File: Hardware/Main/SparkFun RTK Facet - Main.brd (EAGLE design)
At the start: 60 x 43 mm, 126 parts, among them J1 QWIIC_RIGHT_ANGLE, J2 U.FL, J9 CORTEX_JTAG_DEBUG_PTH, Q2 MBT3904DW1T1, Q3 SIL2308, U1 74HC4052D, U10 MCP73833, U12 AP2112K-3.3, U2 3.3V, U3 U-BLOX_ZED-F9P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

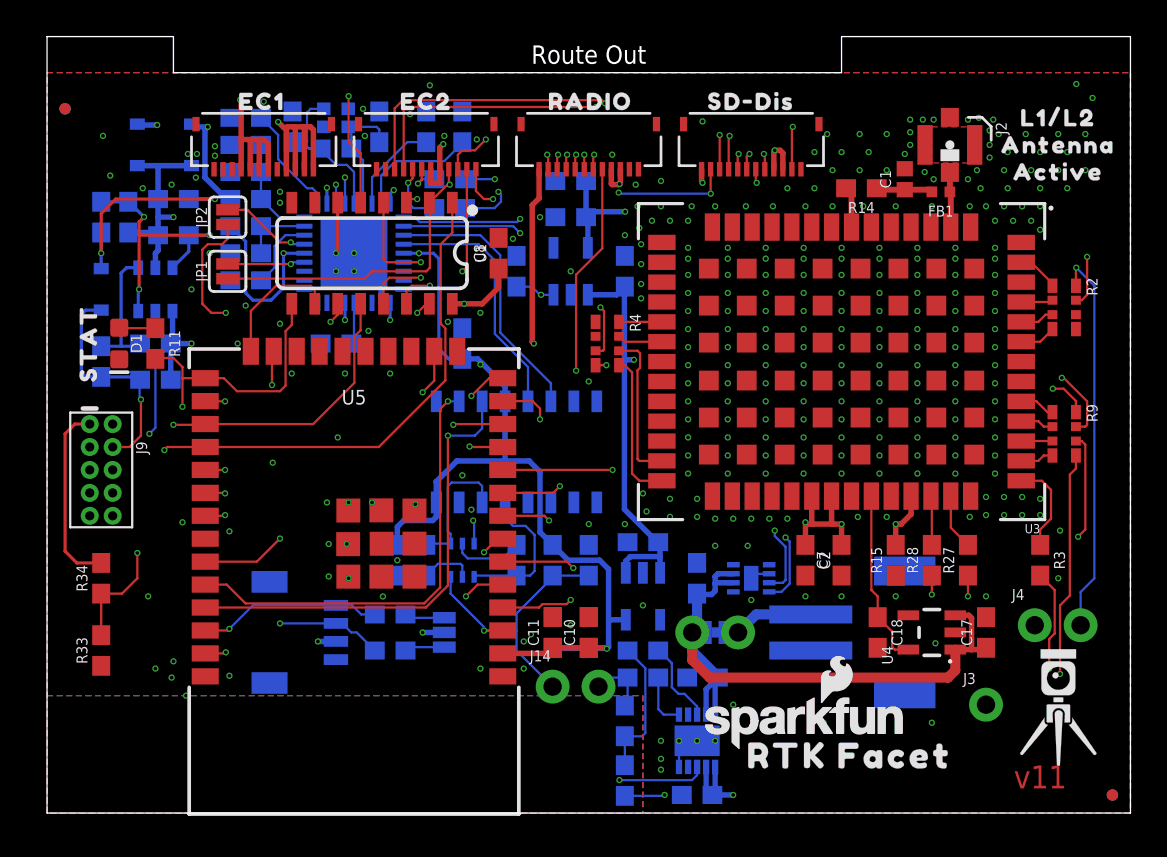
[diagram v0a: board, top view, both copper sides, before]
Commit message: Reduce Main, Connector, Display, and Cell board widths by 1mm to allow for v-score protrusion.
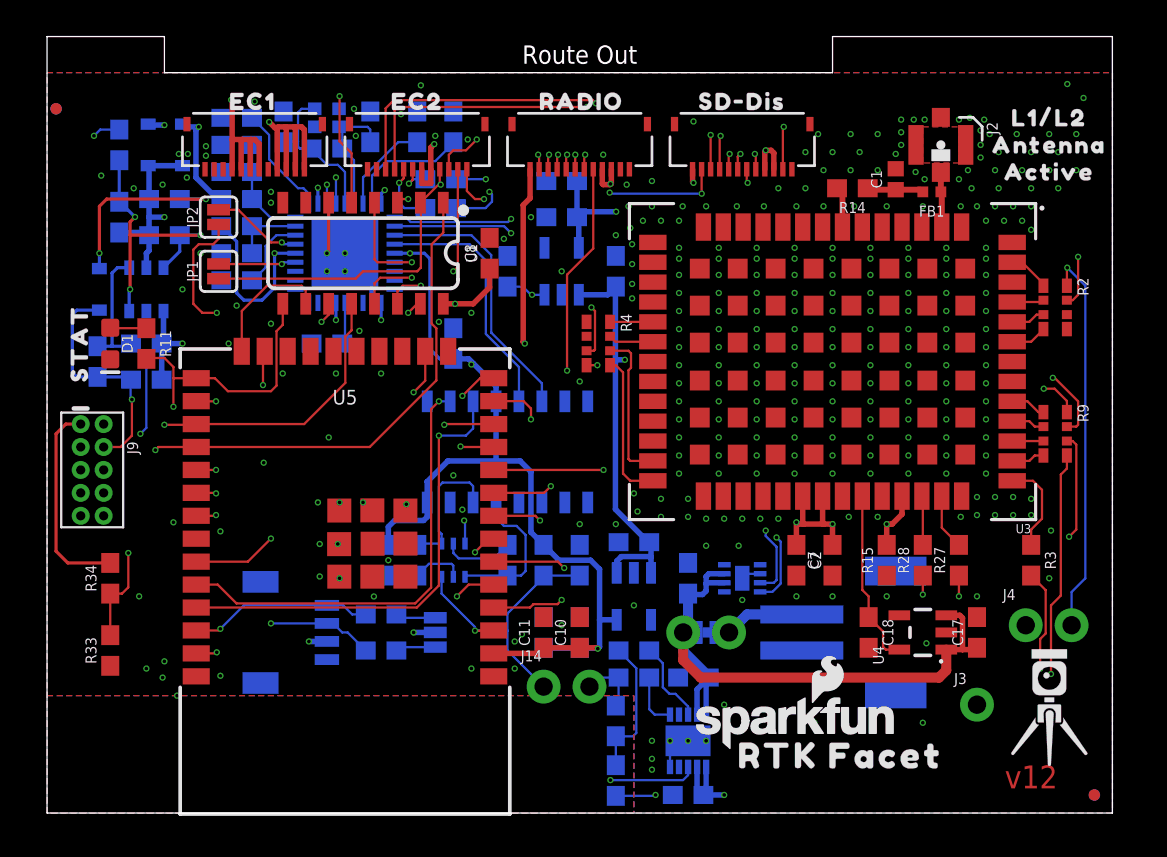
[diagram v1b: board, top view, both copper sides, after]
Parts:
- moved C23 4.12 mm to (4.00, 37.0), turned to 270 degrees
- moved JP21 1.00 mm to (58.0, 1.00)
- moved JP71 1.00 mm to (58.0, 1.00)
- moved D7 0.60 mm to (5.60, 37.0)
- moved C1 0.50 mm to (47.0, 35.1)
- moved C10 0.50 mm to (29.5, 10.0)
- moved C11 0.50 mm to (27.5, 10.0)
- moved C12 0.50 mm to (29.5, 14.0)
- moved C13 0.50 mm to (18.9, 14.0)
- moved C14 0.50 mm to (22.5, 26.0)
- moved C15 0.50 mm to (35.5, 13.0)
- moved C16 0.50 mm to (35.5, 1.00)
- moved C17 0.50 mm to (51.5, 10.0)
- moved C18 0.50 mm to (45.5, 10.0)
- moved C19 0.50 mm to (13.1, 38.0)
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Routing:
- net V_RAW: track 78.3 -> 77.2 mm
- net ESP_3V3: track 118.6 -> 119.6 mm
- net N$6: track 15.3 -> 16.1 mm
- net ESP_I35/DEVICE_SENSE: track 27.4 -> 26.7 mm
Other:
- board size 60 x 43 mm -> 59 x 43 mm
- board text added: "v12"
- board text removed: "v11"

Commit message: Add revisions to schematics. Add PDFs of schematics.
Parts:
- moved FRAME1 0.62 mm to (82.5, 6.35)
- moved FRAME2 0.62 mm to (82.5, 6.35)
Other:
- board text added: "N. Seidle"
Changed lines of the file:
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@@
 <layers>
 <layer number="1" name="Top/Horz" color="4" fill="1" visible="yes" active="yes"/>
-<layer number="2" name="GND/Horz" color="1" fill="3" visible="yes" active="yes"/>
-<layer number="15" name="3.3V/Vert" color="4" fill="6" visible="yes" active="yes"/>
+<layer number="2" name="GND/Horz" color="1" fill="3" visible="no" active="yes"/>
+<layer number="15" name="3.3V/Vert" color="4" fill="6" visible="no" active="yes"/>
 <layer number="16" name="Bottom/Vert" color="1" fill="1" visible="yes" active="yes"/>
 <layer number="17" name="Pads" color="2" fill="1" visible="yes" active="yes"/>
@@
 <layer number="23" name="tOrigins" color="15" fill="1" visible="yes" active="yes"/>
 <layer number="24" name="bOrigins" color="15" fill="1" visible="yes" active="yes"/>
-<layer number="25" name="tNames" color="7" fill="1" visible="yes" active="yes"/>
-<layer number="26" name="bNames" color="7" fill="1" visible="yes" active="yes"/>
-<layer number="27" name="tValues" color="7" fill="1" visible="yes" active="yes"/>
-<layer number="28" name="bValues" color="7" fill="1" visible="yes" active="yes"/>
-<layer number="29" name="tStop" color="7" fill="3" visible="yes" active="yes"/>
-<layer number="30" name="bStop" color="7" fill="6" visible="yes" active="yes"/>
-<layer number="31" name="tCream" color="7" fill="4" visible="yes" active="yes"/>
-<layer number="32" name="bCream" color="7" fill="5" visible="yes" active="yes"/>
-<layer number="33" name="tFinish" color="6" fill="3" visible="yes" active="yes"/>
-<layer number="34" name="bFinish" color="6" fill="6" visible="yes" active="yes"/>
-<layer number="35" name="tGlue" color="7" fill="4" visible="yes" active="yes"/>
-<layer number="36" name="bGlue" color="7" fill="5" visible="yes" active="yes"/>
-<layer number="37" name="tTest" color="7" fill="1" visible="yes" active="yes"/>
-<layer number="38" name="bTest" color="7" fill="1" visible="yes" active="yes"/>
-<layer number="39" name="tKeepout" color="4" fill="11" visible="yes" active="yes"/>
-<layer number="40" name="bKeepout" color="1" fill="11" visible="yes" active="yes"/>
-<layer number="41" name="tRestrict" color="4" fill="10" visible="yes" active="yes"/>
-<layer number="42" name="bRestrict" color="1" fill="10" visible="yes" active="yes"/>
-<layer number="43" name="vRestrict" color="2" fill="10" visible="yes" active="yes"/>
-<layer number="44" name="Drills" color="7" fill="1" visible="yes" active="yes"/>
+<layer number="25" name="tNames" color="7" fill="1" visible="no" active="yes"/>
+<layer number="26" name="bNames" color="7" fill="1" visible="no" active="yes"/>
+<layer number="27" name="tValues" color="7" fill="1" visible="no" active="yes"/>
+<layer number="28" name="bValues" color="7" fill="1" visible="no" active="yes"/>
+<layer number="29" name="tStop" color="7" fill="3" visible="no" active="yes"/>
+<layer number="30" name="bStop" color="7" fill="6" visible="no" active="yes"/>
+<layer number="31" name="tCream" color="7" fill="4" visible="no" active="yes"/>
+<layer number="32" name="bCream" color="7" fill="5" visible="no" active="yes"/>
+<layer number="33" name="tFinish" color="6" fill="3" visible="no" active="yes"/>
+<layer number="34" name="bFinish" color="6" fill="6" visible="no" active="yes"/>
+<layer number="35" name="tGlue" color="7" fill="4" visible="no" active="yes"/>
+<layer number="36" name="bGlue" color="7" fill="5" visible="no" active="yes"/>
+<layer number="37" name="tTest" color="7" fill="1" visible="no" active="yes"/>
+<layer number="38" name="bTest" color="7" fill="1" visible="no" active="yes"/>
+<layer number="39" name="tKeepout" color="4" fill="11" visible="no" active="yes"/>
+<layer number="40" name="bKeepout" color="1" fill="11" visible="no" active="yes"/>
+<layer number="41" name="tRestrict" color="4" fill="10" visible="no" active="yes"/>
+<layer number="42" name="bRestrict" color="1" fill="10" visible="no" active="yes"/>
+<layer number="43" name="vRestrict" color="2" fill="10" visible="no" active="yes"/>
+<layer number="44" name="Drills" color="7" fill="1" visible="no" active="yes"/>
 <layer number="45" name="Holes" color="7" fill="1" visible="yes" active="yes"/>
-<layer number="46" name="Milling" color="3" fill="1" visible="yes" active="yes"/>
-<layer number="47" name="Measures" color="7" fill="1" visible="yes" active="yes"/>
-<layer number="48" name="Document" color="7" fill="1" visible="yes" active="yes"/>
-<layer number="49" name="Reference" color="7" fill="1" visible="yes" active="yes"/>
-<layer number="50" name="dxf" color="7" fill="1" visible="yes" active="yes"/>
+<layer number="46" name="Milling" color="3" fill="1" visible="no" active="yes"/>
+<layer number="47" name="Measures" color="7" fill="1" visible="no" active="yes"/>
+<layer number="48" name="Document" color="7" fill="1" visible="no" active="yes"/>
+<layer number="49" name="Reference" color="7" fill="1" visible="no" active="yes"/>
+<layer number="50" name="dxf" color="7" fill="1" visible="no" active="yes"/>
 <layer number="51" name="tDocu" color="6" fill="1" visible="yes" active="yes"/>
-<layer number="52" name="bDocu" color="7" fill="1" visible="yes" active="yes"/>
+<layer number="52" name="bDocu" color="7" fill="1" visible="no" active="yes"/>
 <layer number="91" name="Nets" color="2" fill="1" visible="no" active="no"/>
 <layer number="92" name="Busses" color="1" fill="1" visible="no" active="no"/>
@@
 <text x="29.5" y="42" size="1.016" layer="20" font="vector" ratio="15" align="center">Route Out</text>
 <text x="63.81" y="60.96" size="1.778" layer="51" font="vector" ratio="15">Impedance controlled: JLC7628</text>
+<text x="113.03" y="6.35" size="1.778" layer="51" font="vector" ratio="15">N. Seidle</text>
 </plain>
 <attributes>
@@
 </element>
 <element name="U$30" library="SparkFun-Aesthetics" package="QWIIC_4MM" value="" x="13" y="14.6" smashed="yes" rot="MR0"/>
-<element name="FRAME2" library="SparkFun-Aesthetics" package="CREATIVE_COMMONS" value="FRAME-LEDGER" x="82.04" y="6" smashed="yes">
-<attribute name="DESIGNER" value="" x="82.04" y="6" size="1.778" layer="27" font="vector" ratio="15" display="off"/>
-<attribute name="REV" value="" x="82.04" y="6" size="1.778" layer="27" font="vector" ratio="15" display="off"/>
+<element name="FRAME2" library="SparkFun-Aesthetics" package="CREATIVE_COMMONS" value="FRAME-LEDGER" x="82.55" y="6.35" smashed="yes">
+<attribute name="DESIGNER" value="" x="82.55" y="6.35" size="1.778" layer="27" font="vector" ratio="15" display="off"/>
+<attribute name="REV" value="" x="82.55" y="6.35" size="1.778" layer="27" font="vector" ratio="15" display="off"/>
 </element>
 <element name="R9" library="SparkFun-Resistors" package="1206_RA" value="33" x="55.8" y="21" smashed="yes" rot="R270">
@@
 <attribute name="VALUE" x="6.5" y="33.238" size="0.6096" layer="28" font="vector" ratio="20" rot="MR0" align="top-center"/>
 </element>
-<element name="FRAME1" library="SparkFun-Aesthetics" package="CREATIVE_COMMONS" value="FRAME-LEDGER" x="82.04" y="6" smashed="yes">
-<attribute name="DESIGNER" value="" x="82.04" y="6" size="1.778" layer="27" font="vector" ratio="15" display="off"/>
-<attribute name="REV" value="" x="82.04" y="6" size="1.778" layer="27" font="vector" ratio="15" display="off"/>
+<element name="FRAME1" library="SparkFun-Aesthetics" package="CREATIVE_COMMONS" value="FRAME-LEDGER" x="82.55" y="6.35" smashed="yes">
+<attribute name="DESIGNER" value="" x="82.55" y="6.35" size="1.778" layer="27" font="vector" ratio="15" display="off"/>
+<attribute name="REV" value="" x="82.55" y="6.35" size="1.778" layer="27" font="vector" ratio="15" display="off"/>
 </element>
 <element name="D7" library="SparkFun-DiscreteSemi" package="SOD-323" value="3A/10V/280mV" x="5.6" y="37" smashed="yes" rot="MR90">

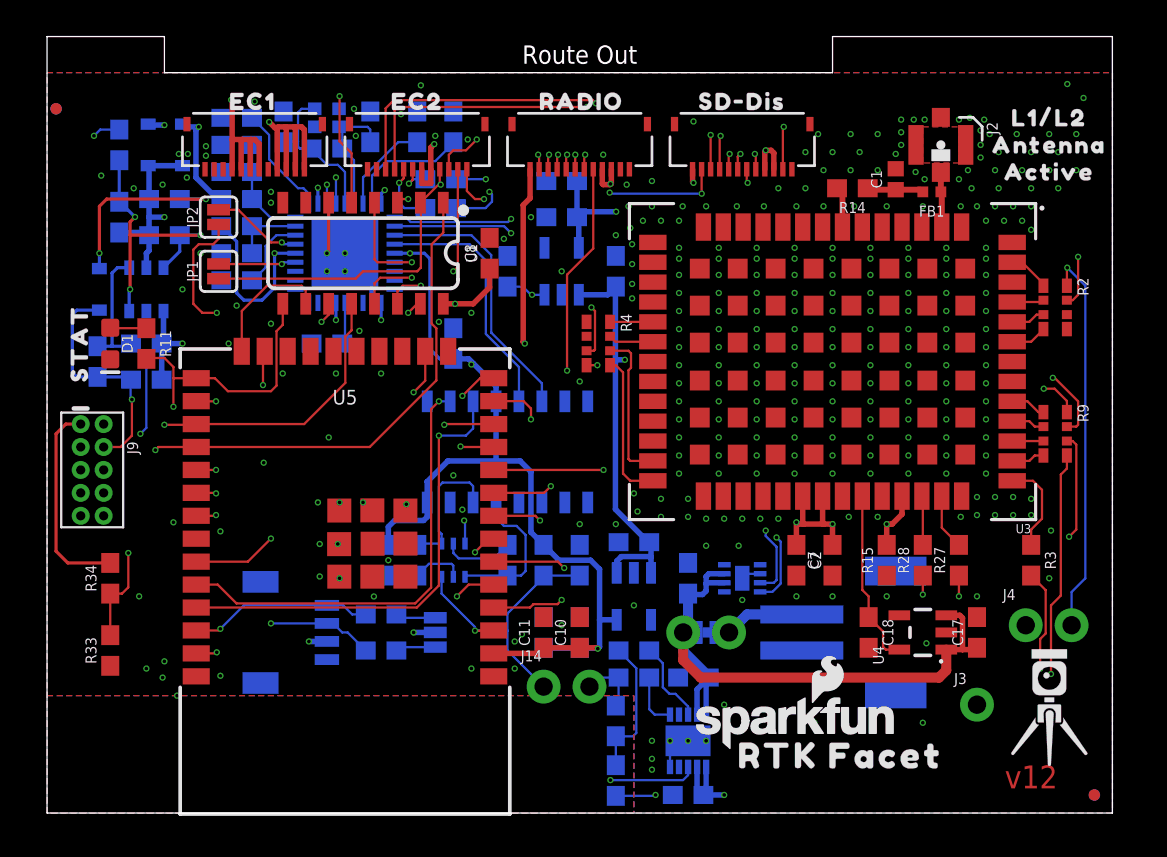
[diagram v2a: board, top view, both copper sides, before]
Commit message: Move thermistor from heat sources.
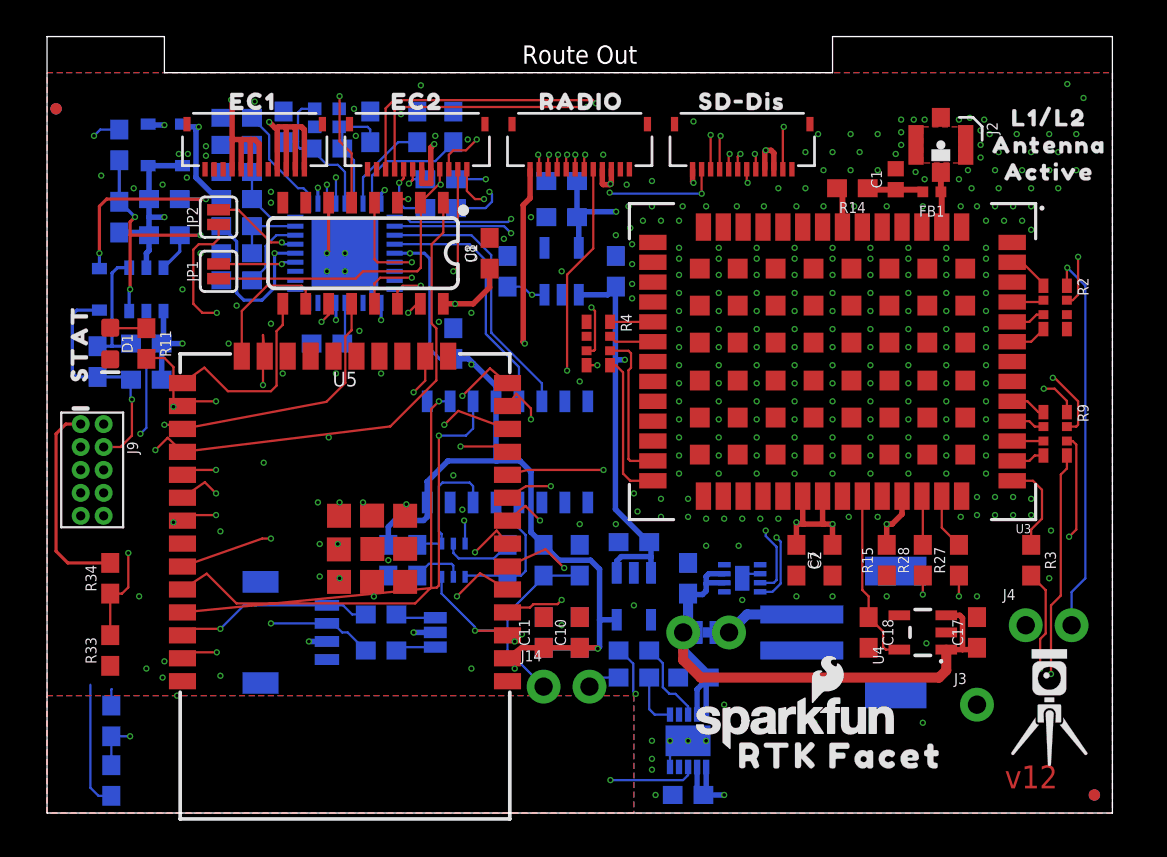
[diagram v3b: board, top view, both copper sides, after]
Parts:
- U5: value ESP-WROOM-3232D-NARROW -> ESP-WROOM-3232D; device SparkFun-RF:ESP-WROOM-32D-NARROW -> SparkFun-RF:ESP-WROOM-32D
- moved R10 27.9 mm to (3.56, 1.80)
- moved R30 27.9 mm to (3.56, 5.10)
- moved U5 1.00 mm to (16.5, 15.0)
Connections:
- net GND: now also U5.GND; no longer U5.GND1
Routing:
- net CHG_THERM1: track 7.78 -> 34.5 mm, vias 0 -> 2
- net GND: track 14.9 -> 19.1 mm
- net ESP_15/MTDO/RADIO_!RESET!: track 44.2 -> 46.2 mm
- net ESP_I35/DEVICE_SENSE: track 26.7 -> 27.9 mm
- net ESP_12/MTDI: track 26.5 -> 27.8 mm
- net ESP_18/SD_SCK: track 51.6 -> 52.9 mm
- net ESP32_RXI: track 24.9 -> 26.2 mm
- net ESP_I39/ADC39: track 32.4 -> 33.6 mm
- net ESP_27/FAST_OFF: track 32.3 -> 33.6 mm
- net ESP_4/RADIO_PWR_ON: track 38.4 -> 39.3 mm
- net ESP32_EN: track 43.9 -> 44.9 mm
- net ESP_5/RADIO_CTSI: track 41.8 -> 42.7 mm
- net ESP_19/SD_CIPO: track 54.1 -> 55.0 mm
- net ESP_23/SD_COPI: track 62.5 -> 63.3 mm
- net ESP_22/SCL: track 140.5 -> 141.3 mm
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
